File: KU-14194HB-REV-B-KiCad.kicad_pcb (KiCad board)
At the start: 2 copper layers, 387.7 x 180.3 mm, 36 parts, among them U1 CIA_U1, U2 CIA_U2, U20 556, U27 7408_U27, U28 4066_U28, U7 6510_MPU, U8 7406N

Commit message: schematics update
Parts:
- added CN2: USER_PORT_CON, KU-14194HB-RevB-KiCad:EDGE_CON_24P, F.Cu at (39.1, 51.4)
- added FB5: FERRITE_NARROW, KU-14194HB-RevB-KiCad:RECTIFIER, F.Cu at (92.7, 116.8)
- added RP4: R_ARRAY_9WAY_US, KU-14194HB-RevB-KiCad:RP_ARRAY_9WAY, F.Cu at (312.4, 94.0)
- RP3: value R_US_ARRAY -> R_ARRAY_7WAY_US; footprint Resistor_THT:R_Array_SIP8 -> KU-14194HB-RevB-KiCad:RP_ARRAY_7WAY
- moved C2 204.4 mm to (43.2, 73.7), turned to 180 degrees
- moved C96 193.0 mm to (83.8, 71.1), turned to 270 degrees
- moved C3 192.7 mm to (68.6, 73.7)
- moved C9 173.5 mm to (205.7, 73.7), turned to 180 degrees
- moved FB18 32.2 mm to (189.2, 236.2)
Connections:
- net Net-(U1-Pad23) renamed ~CIA1~
- net Net-(U2-Pad2) renamed ~VA14~
- net Net-(U2-Pad23) renamed ~CIA2~
- net Net-(U2-Pad3) renamed ~VA15~
- net Net-(U7-Pad11) renamed /Sheet1/A4
- net Net-(U7-Pad12) renamed /Sheet1/A5
- net Net-(U7-Pad13) renamed /Sheet1/A6
- net Net-(U7-Pad14) renamed /Sheet1/A7
- net Net-(U7-Pad15) renamed /Sheet1/A8
- net Net-(U7-Pad16) renamed /Sheet1/A9
- net Net-(U7-Pad17) renamed /Sheet1/A10
- net Net-(U7-Pad18) renamed /Sheet1/A11
- net Net-(U7-Pad2) renamed RDY
- U1 pad 21: Net-(U1-Pad21) -> ~IRQ~
- U1 pad 22: Net-(U1-Pad22) -> R\~W~
- U1 pad 25: Net-(U1-Pad25) -> PHI2
- U1 pad 26: Net-(U1-Pad26) -> /Sheet1/D7
- U1 pad 27: Net-(U1-Pad27) -> /Sheet1/D6
- U1 pad 28: Net-(U1-Pad28) -> /Sheet1/D5
- U1 pad 29: Net-(U1-Pad29) -> /Sheet1/D4
- U1 pad 30: Net-(U1-Pad30) -> /Sheet1/D3
- U1 pad 31: Net-(U1-Pad31) -> /Sheet1/D2
- U1 pad 32: Net-(U1-Pad32) -> /Sheet1/D1
- U1 pad 33: Net-(U1-Pad33) -> /Sheet1/D0
- U1 pad 35: Net-(U1-Pad35) -> /Sheet1/A3
- U1 pad 36: Net-(U1-Pad36) -> /Sheet1/A2
- U1 pad 37: Net-(U1-Pad37) -> /Sheet1/A1
- U1 pad 38: Net-(U1-Pad38) -> /Sheet1/A0
- U2 pad 22: Net-(U2-Pad22) -> R\~W~
- U2 pad 25: Net-(U2-Pad25) -> PHI2
- U2 pad 26: Net-(U2-Pad26) -> /Sheet1/D7
- U2 pad 27: Net-(U2-Pad27) -> /Sheet1/D6
- U2 pad 28: Net-(U2-Pad28) -> /Sheet1/D5
- U2 pad 29: Net-(U2-Pad29) -> /Sheet1/D4
- U2 pad 30: Net-(U2-Pad30) -> /Sheet1/D3
- U2 pad 31: Net-(U2-Pad31) -> /Sheet1/D2
- U2 pad 32: Net-(U2-Pad32) -> /Sheet1/D1
- U2 pad 33: Net-(U2-Pad33) -> /Sheet1/D0
- U2 pad 35: Net-(U2-Pad35) -> /Sheet1/A3
- U2 pad 36: Net-(U2-Pad36) -> /Sheet1/A2
- U2 pad 37: Net-(U2-Pad37) -> /Sheet1/A1
- U2 pad 38: Net-(U2-Pad38) -> /Sheet1/A0
- U7 pad 10: Net-(U7-Pad10) -> /Sheet1/A3
- U7 pad 19: Net-(U7-Pad19) -> /Sheet1/A12
- U7 pad 20: Net-(U7-Pad20) -> /Sheet1/A13
- U7 pad 22: Net-(U7-Pad22) -> /Sheet1/A14
- U7 pad 23: Net-(U7-Pad23) -> /Sheet1/A15
- U7 pad 3: Net-(U7-Pad3) -> ~IRQ~
- U7 pad 30: Net-(U7-Pad30) -> /Sheet1/D7
- U7 pad 31: Net-(U7-Pad31) -> /Sheet1/D6
- U7 pad 32: Net-(U7-Pad32) -> /Sheet1/D5
- U7 pad 33: Net-(U7-Pad33) -> /Sheet1/D4
- U7 pad 34: Net-(U7-Pad34) -> /Sheet1/D3
- U7 pad 35: Net-(U7-Pad35) -> /Sheet1/D2
- U7 pad 36: Net-(U7-Pad36) -> /Sheet1/D1
- U7 pad 37: Net-(U7-Pad37) -> /Sheet1/D0
- U7 pad 38: Net-(U7-Pad38) -> R\~W~
- U7 pad 39: Net-(U7-Pad39) -> /Sheet1/PH2_FB
- U7 pad 7: Net-(U7-Pad7) -> /Sheet1/A0
- U7 pad 8: Net-(U7-Pad8) -> /Sheet1/A1
- U7 pad 9: Net-(U7-Pad9) -> /Sheet1/A2
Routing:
- net (no net): track 17856.9 -> 16447.7 mm, vias 737 -> 715
- net Net-(U1-Pad33): track 640.6 -> 0.00 mm, vias 15 -> 0
- net /Sheet1/D0: track 0.00 -> 640.6 mm, vias 0 -> 15
- net R\~W~: track 0.00 -> 638.7 mm, vias 0 -> 21
- net Net-(U1-Pad22): track 638.7 -> 0.00 mm, vias 21 -> 0
- net Net-(U1-Pad31): track 609.7 -> 0.00 mm, vias 16 -> 0
- net /Sheet1/D2: track 0.00 -> 609.7 mm, vias 0 -> 16
- net Net-(U1-Pad32): track 599.1 -> 0.00 mm, vias 15 -> 0
- net /Sheet1/D1: track 0.00 -> 599.1 mm, vias 0 -> 15
- net PHI2: track 0.00 -> 596.8 mm, vias 0 -> 7
- net Net-(U1-Pad25): track 596.8 -> 0.00 mm, vias 8 -> 0
- net Net-(U1-Pad38): track 557.4 -> 0.00 mm, vias 17 -> 0
- net /Sheet1/A0: track 0.00 -> 557.4 mm, vias 0 -> 17
- net Net-(U1-Pad36): track 549.0 -> 0.00 mm, vias 16 -> 0
- net /Sheet1/A2: track 0.00 -> 549.0 mm, vias 0 -> 16
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
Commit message: more connectors and stuff
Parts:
- added C1: .1, KU-14194HB-RevB-KiCad:CAP_P5.08mm, F.Cu at (142.2, 71.1)
- added C100: .22, KU-14194HB-RevB-KiCad:CAP_P5.08mm, F.Cu at (381.0, 63.5)
- added C102: 10uF, KU-14194HB-RevB-KiCad:CAP_ELYT_RADIAL_P2.54mm, F.Cu at (363.2, 134.6)
- added C103: .1, KU-14194HB-RevB-KiCad:CAP_P5.08mm, F.Cu at (363.2, 139.7)
- added C18: .1, KU-14194HB-RevB-KiCad:CAP_P5.08mm, F.Cu at (322.6, 104.1)
- added C19: 2200uF, KU-14194HB-RevB-KiCad:LARGE_ELECTROLYTIC_33x18_P38.10mm_AXIAL_TH, F.Cu at (375.9, 132.1)
- added C20: .22, KU-14194HB-RevB-KiCad:CAP_POLY_100V_TH_P10.16mm, F.Cu at (363.2, 88.9)
- added C21: .22, KU-14194HB-RevB-KiCad:CAP_POLY_100V_TH_P10.16mm, F.Cu at (368.3, 114.3)
- added C57: 10uF, KU-14194HB-RevB-KiCad:CAP_ELYT_RADIAL_P2.54mm, F.Cu at (302.3, 203.2)
- added C59: .1, KU-14194HB-RevB-KiCad:CAP_P5.08mm, F.Cu at (297.2, 203.2)
- added C8: 10uF, KU-14194HB-RevB-KiCad:CAP_ELYT_RADIAL_P2.54mm, F.Cu at (193.0, 73.7)
- added C88: 1000uF, KU-14194HB-RevB-KiCad:LARGE_ELECTROLYTIC_33x18_P38.10mm_AXIAL_TH, F.Cu at (350.5, 208.3)
- added C89: .1, KU-14194HB-RevB-KiCad:CAP_P5.08mm, F.Cu at (330.2, 196.8)
- added C90: 470uF, KU-14194HB-RevB-KiCad:LARGE_ELECTROLYTIC_33x18_P38.10mm_AXIAL_TH, F.Cu at (368.3, 208.3)
- added C91: 100uF, KU-14194HB-RevB-KiCad:CAP_ELYT_RADIAL_P5.08mm, F.Cu at (391.2, 205.7)
- added C92: .1, KU-14194HB-RevB-KiCad:CAP_P5.08mm, F.Cu at (391.2, 198.1)
- added C95: .1, KU-14194HB-RevB-KiCad:CAP_P5.08mm, F.Cu at (378.5, 127.0)
- added C97: .22, KU-14194HB-RevB-KiCad:CAP_P5.08mm, F.Cu at (381.0, 68.6)
- added C98: .1, KU-14194HB-RevB-KiCad:CAP_P5.08mm, F.Cu at (383.5, 106.7)
- added C99: .1, KU-14194HB-RevB-KiCad:CAP_P5.08mm, F.Cu at (378.5, 101.6)
- added CN1: KEYBOARD_20PIN_MALE, KU-14194HB-RevB-KiCad:KEYBOARD_CON, F.Cu at (27.9, 129.5)
- added CN3: CASSETTE_PORT_CON, KU-14194HB-RevB-KiCad:EDGE_CON_12P_TAPE, F.Cu at (124.5, 51.5)
- added CN4: SERIAL_BUS_CON, KU-14194HB-RevB-KiCad:SERIAL_CON_DIN6, F.Cu at (180.3, 58.9)
- added CN7: POWER_CON, KU-14194HB-RevB-KiCad:POWER_CON_DIN7, F.Cu at (393.4, 71.6)
- added CN8: CONTROL_PORT, KU-14194HB-RevB-KiCad:JOYPORT_DB9, F.Cu at (391.5, 112.2)
- added CN9: CONTROL_PORT, KU-14194HB-RevB-KiCad:JOYPORT_DB9, F.Cu at (391.5, 144.0)
- added CR2: IN755, KU-14194HB-RevB-KiCad:ZENER_12.7mm, F.Cu at (330.2, 99.1)
- added CR5: 1N4001, KU-14194HB-RevB-KiCad:RECTIFIER_TH_P12.7mm, F.Cu at (335.3, 193.0)
- added CR6: 1N4001, KU-14194HB-RevB-KiCad:RECTIFIER_TH_P12.7mm, F.Cu at (337.8, 205.7)
- added FB1: FERRITE_NARROW, KU-14194HB-RevB-KiCad:FERRITE_BEAD_TH_P12.7mm, F.Cu at (108.0, 76.2)
- added FB2: FERRITE_NARROW, KU-14194HB-RevB-KiCad:FERRITE_BEAD_TH_P12.7mm, F.Cu at (153.7, 71.1)
- added FB20: FERRITE_NARROW, KU-14194HB-RevB-KiCad:FERRITE_BEAD_TH_P12.7mm, F.Cu at (384.8, 188.0)
- added FB21: FERRITE_NARROW, KU-14194HB-RevB-KiCad:FERRITE_BEAD_TH_P12.7mm, F.Cu at (384.8, 182.9)
- added FB3: FERRITE_NARROW, KU-14194HB-RevB-KiCad:FERRITE_BEAD_TH_P12.7mm, F.Cu at (135.9, 76.2)
- added Q1: 2SC1815, KU-14194HB-RevB-KiCad:Q_NPN_ECB, F.Cu at (312.4, 106.7)
- added Q2: 2SC1815, KU-14194HB-RevB-KiCad:Q_NPN_ECB, F.Cu at (335.3, 109.2)
- added Q3: TP298/2SD880, Package_TO_SOT_THT:TO-220-3_Vertical, F.Cu at (307.3, 109.2)
- added R1: 3K3, KU-14194HB-RevB-KiCad:RESISTOR, F.Cu at (124.5, 71.1)
- added R2: 1.5K, KU-14194HB-RevB-KiCad:RESISTOR, F.Cu at (327.7, 99.1)
- added R3: 10K, KU-14194HB-RevB-KiCad:RESISTOR, F.Cu at (342.9, 99.1)
- added R39: 390, KU-14194HB-RevB-KiCad:RESISTOR, F.Cu at (391.2, 193.0)
- added R4: 1K, KU-14194HB-RevB-KiCad:RESISTOR, F.Cu at (340.4, 99.1)
- added R43: 3K3, KU-14194HB-RevB-KiCad:RESISTOR, F.Cu at (147.3, 134.6)
- added R44: 3K3, KU-14194HB-RevB-KiCad:RESISTOR, F.Cu at (147.3, 137.2)
- added R45: 3K3, KU-14194HB-RevB-KiCad:RESISTOR, F.Cu at (147.3, 139.7)
- added VR1: 7812, KU-14194HB-RevB-KiCad:VOTLAGE_REGULATOR_TO220, F.Cu at (309.9, 203.2)
- added VR2: 7805, KU-14194HB-RevB-KiCad:VOTLAGE_REGULATOR_TO220, F.Cu at (373.4, 119.4)
- FB18, FB5, FB7, FB8, FB9: footprint KU-14194HB-RevB-KiCad:RECTIFIER -> KU-14194HB-RevB-KiCad:FERRITE_BEAD_TH_P12.7mm
- moved FB18 204.1 mm to (384.8, 177.8), turned to 180 degrees
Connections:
- net Net-(U7-Pad5) renamed CAEC
- CN2 pad N: (no net) -> Earth
- FB18 pad 2: Net-(CN8-Pad7) -> /Sheet1/5V_joyport
- R36 pad 2: ~RESET~ -> Net-(R36-Pad2)
- U7 pad 24: Net-(U7-Pad24) -> /Sheet1/CASS_MOTOR
- U7 pad 25: Net-(U7-Pad25) -> /Sheet1/CASS_SENSE
- U7 pad 26: Net-(U7-Pad26) -> /Sheet1/CASS_WRT
- U7 pad 27: Net-(U7-Pad27) -> ~CHAREN~
- U7 pad 28: Net-(U7-Pad28) -> ~HIRAM~
- U7 pad 29: Net-(U7-Pad29) -> ~LORAM~
- U8 pad 12: ~RESET~ -> Net-(R36-Pad2)
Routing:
- net (no net): track 16447.7 -> 12520.7 mm, vias 715 -> 556
- net /Sheet1/+9V_UNREG: track 0.00 -> 1275.8 mm, vias 0 -> 49
- net Earth: track 5302.7 -> 4815.6 mm, vias 115 -> 119
- net +5V: track 3523.6 -> 3809.9 mm, vias 107 -> 97
- net Net-(U7-Pad25): track 210.6 -> 0.00 mm, vias 3 -> 0
- net /Sheet1/CASS_SENSE: track 0.00 -> 189.6 mm, vias 0 -> 2
- net Net-(FB2-Pad2): track 0.00 -> 175.0 mm, vias 0 -> 3
- net Net-(U7-Pad26): track 153.9 -> 0.00 mm, vias 2 -> 0
- net /Sheet1/CASS_WRT: track 0.00 -> 153.9 mm, vias 0 -> 1
- net /Sheet1/CAN+5V: track 0.00 -> 144.6 mm, vias 0 -> 6
- net +9V_UNREG: track 0.00 -> 142.4 mm, vias 0 -> 6
- net Net-(U7-Pad24): track 142.2 -> 0.00 mm, vias 2 -> 0
- net /Sheet1/CASS_MOTOR: track 0.00 -> 142.2 mm, vias 0 -> 1
- net +12V: track 0.00 -> 132.6 mm, vias 0 -> 5
- net /Sheet1/9V_UNREG: track 0.00 -> 126.3 mm
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- added copper zone on F.Cu, net Earth

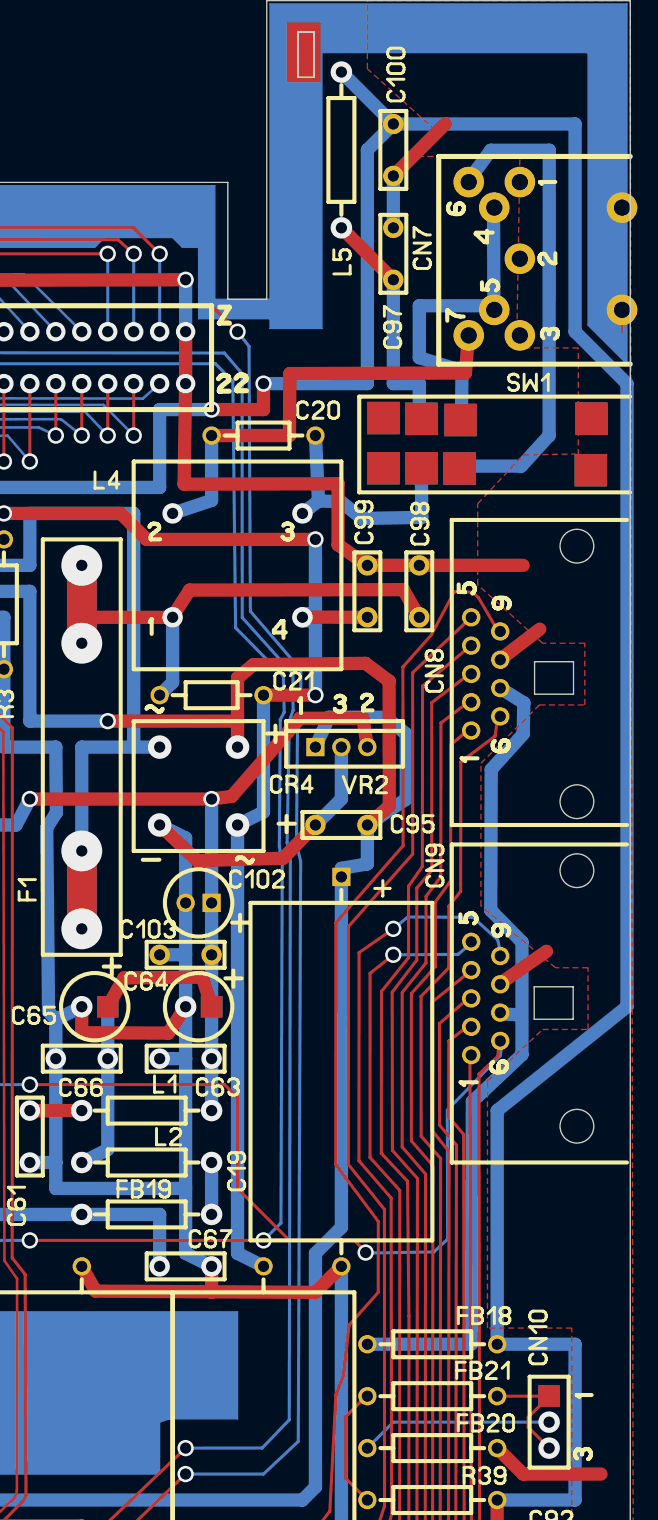
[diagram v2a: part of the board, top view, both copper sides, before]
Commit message: added missing parts. powre connector is upside down in the ku board
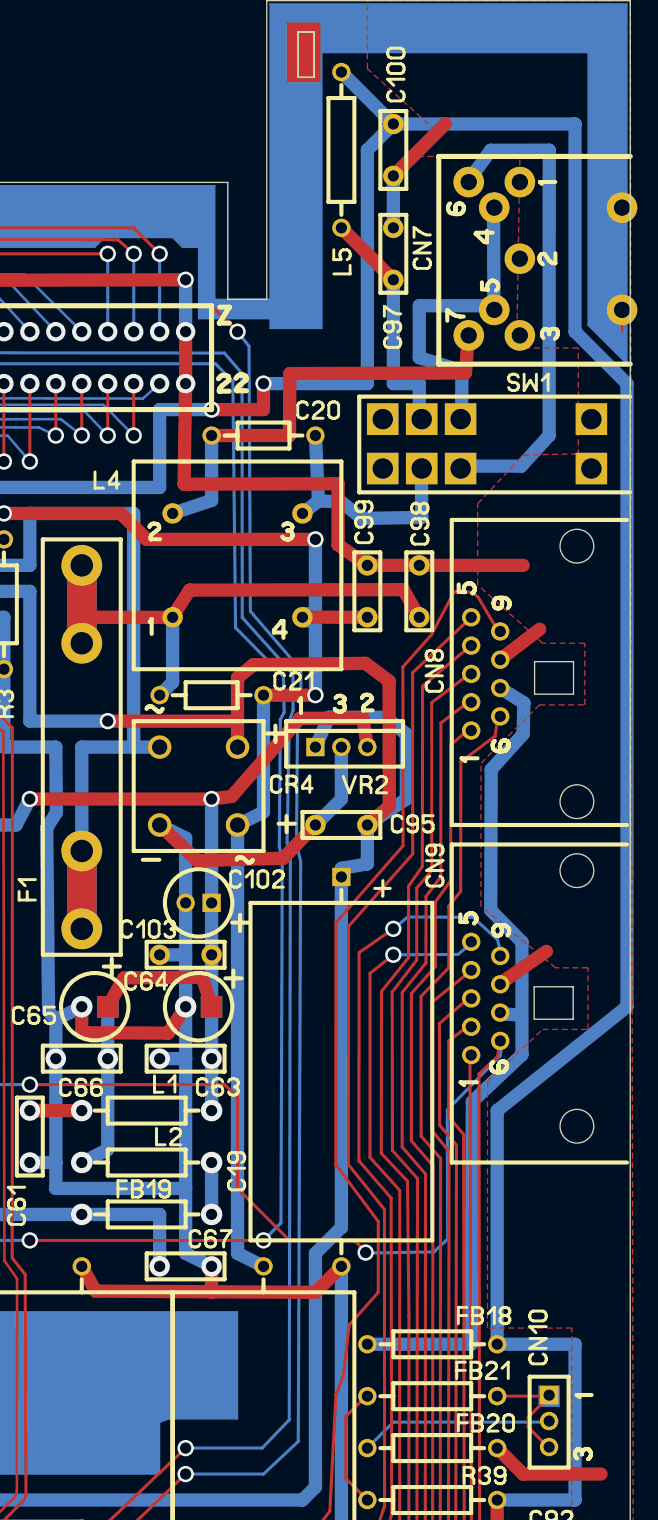
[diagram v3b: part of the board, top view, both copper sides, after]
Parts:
- added CN10: LED_CONNECTOR, KU-14194HB-RevB-KiCad:LED_CON, F.Cu at (396.2, 182.8)
- added CR4: BRIDGE_RECTIFIER, KU-14194HB-RevB-KiCad:BRIDGE_RECTIFIER, F.Cu at (365.8, 119.4)
- added F1: 1A, KU-14194HB-RevB-KiCad:FUSE, F.Cu at (350.5, 137.2)
- added L4: CHOKE, KU-14194HB-RevB-KiCad:CHOKE, F.Cu at (359.4, 106.7)
- added L5: 1.2uH, KU-14194HB-RevB-KiCad:INDUCTOR_P15.24mm, F.Cu at (375.9, 53.3)
- added SW1: POWER_SWITCH, KU-14194HB-RevB-KiCad:POWER_SWITCH, F.Cu at (383.8, 92.1)
- moved C20 10.2 mm to (373.4, 88.9), turned to 180 degrees
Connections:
- C20 pad 1: Net-(C20-Pad1) -> /Sheet1/9VAC
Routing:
- net Net-(C97-Pad2): track 23.7 -> 373.9 mm, vias 1 -> 0
- net (no net): track 12520.7 -> 12170.6 mm
- net /Sheet1/9V_UNREG: track 126.3 -> 268.7 mm, vias 0 -> 5
- net +9V_UNREG: track 142.4 -> 0.00 mm, vias 6 -> 0
- net Net-(C20-Pad1): track 44.9 -> 0.00 mm, vias 1 -> 0
- net /Sheet1/9VAC: track 0.00 -> 23.7 mm
- net Net-(C20-Pad2): track 23.7 -> 44.9 mm, vias 1 -> 0
- net Net-(C21-Pad2): vias 3 -> 0
- net Earth: vias 119 -> 118
- net /Sheet1/LED+: vias 1 -> 0
- net /Sheet1/GND_LED: vias 1 -> 0
- net /Sheet1/9VAC~~: vias 9 -> 7
- net /Sheet1/'9VAC~~: vias 6 -> 3
- net +5V: vias 97 -> 96

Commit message: Oscillator area
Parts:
- added C107: 10uF, KU-14194HB-RevB-KiCad:CAP_ELYT_RADIAL_P2.54mm, F.Cu at (317.5, 167.6)
- added C108: 10uF, KU-14194HB-RevB-KiCad:CAP_ELYT_RADIAL_P2.54mm, F.Cu at (299.7, 165.1)
- added C36: .1, KU-14194HB-RevB-KiCad:RESISTOR, F.Cu at (297.2, 180.3)
- added C56: .1, KU-14194HB-RevB-KiCad:CAP_P5.08mm, F.Cu at (325.1, 124.5)
- added C58: .1, KU-14194HB-RevB-KiCad:CAP_P5.08mm, F.Cu at (322.6, 165.1)
- added C65: 10uF, KU-14194HB-RevB-KiCad:CAP_ELYT_RADIAL_P2.54mm, F.Cu at (353.1, 144.8)
- added C66: .1, KU-14194HB-RevB-KiCad:CAP_P5.08mm, F.Cu at (353.1, 149.9)
- added C67: .1, KU-14194HB-RevB-KiCad:CAP_P5.08mm, F.Cu at (358.1, 170.2)
- added C68: .1, KU-14194HB-RevB-KiCad:CAP_P5.08mm, F.Cu at (309.9, 160.0)
- added C70: ~, KU-14194HB-RevB-KiCad:RESISTOR, F.Cu at (317.5, 185.4)
- added C74: .1, KU-14194HB-RevB-KiCad:CAP_P5.08mm, F.Cu at (309.9, 124.5)
- added C83: 82pF, KU-14194HB-RevB-KiCad:RESISTOR, F.Cu at (315.0, 152.4)
- added C84: .1, KU-14194HB-RevB-KiCad:CAP_P5.08mm, F.Cu at (325.1, 149.9)
- added C85: .47, KU-14194HB-RevB-KiCad:CAP_P5.08mm, F.Cu at (335.3, 144.8)
- added C86: ?, KU-14194HB-RevB-KiCad:RESISTOR, F.Cu at (299.7, 185.4)
- added E1: JUMPER_WIRE, KU-14194HB-RevB-KiCad:JUMPER_WIRE, F.Cu at (279.4, 137.2)
- added FB16: FERRITE_NARROW, KU-14194HB-RevB-KiCad:FERRITE_BEAD_TH_P12.7mm, F.Cu at (281.9, 148.6)
- added FB17: FERRITE_NARROW, KU-14194HB-RevB-KiCad:FERRITE_BEAD_TH_P12.7mm, F.Cu at (290.8, 185.4)
- added FB19: FERRITE_NARROW, KU-14194HB-RevB-KiCad:FERRITE_BEAD_TH_P12.7mm, F.Cu at (356.9, 165.1)
- added Q7: 2SC1815, KU-14194HB-RevB-KiCad:Q_NPN_ECB, F.Cu at (327.7, 154.9)
- added R16: 1K, KU-14194HB-RevB-KiCad:RESISTOR, F.Cu at (332.7, 124.5)
- added R17: 2K7, KU-14194HB-RevB-KiCad:RESISTOR, F.Cu at (335.3, 124.5)
- added R19: 15K, KU-14194HB-RevB-KiCad:RESISTOR, F.Cu at (332.7, 152.4)
- added R26: 100, KU-14194HB-RevB-KiCad:RESISTOR, F.Cu at (335.3, 172.7)
- added R27: 500, KU-14194HB-RevB-KiCad:POTMETER, F.Cu at (332.7, 160.0)
- added R52: ?, KU-14194HB-RevB-KiCad:RESISTOR, F.Cu at (335.3, 170.2)
- added R53: ?, KU-14194HB-RevB-KiCad:RESISTOR, F.Cu at (322.6, 167.6)
- added U29: 74LS74, KU-14194HB-RevB-KiCad:DIP14, F.Cu at (290.8, 137.2)
- added U30: 74LS193, KU-14194HB-RevB-KiCad:DIP16, F.Cu at (308.6, 138.4)
- added U31: 74LS629N, KU-14194HB-RevB-KiCad:DIP16, F.Cu at (308.6, 174.0)
- added U32: MC4044, KU-14194HB-RevB-KiCad:DIP14, F.Cu at (323.9, 137.2)
- added Y1: Crystal, KU-14194HB-RevB-KiCad:CRYSTAL, F.Cu at (320.0, 180.3)
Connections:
- R36 pad 2: Net-(R36-Pad2) -> ~RESET~
- U7 pad 1: Net-(U7-Pad1) -> PHI_0
- U8 pad 12: Net-(R36-Pad2) -> ~RESET~
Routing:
- net /Sheet1/+9V_UNREG: track 1275.8 -> 0.00 mm, vias 49 -> 0
- net Earth: track 4815.6 -> 5978.7 mm, vias 118 -> 136
- net (no net): track 12170.6 -> 11054.7 mm, vias 556 -> 442
- net /Sheet1/+Vc: track 0.00 -> 314.6 mm, vias 0 -> 11
- net PHI_0: track 0.00 -> 270.1 mm, vias 0 -> 4
- net Net-(U7-Pad1): track 270.1 -> 0.00 mm, vias 5 -> 0
- net DOT_CLOCK: track 0.00 -> 148.4 mm, vias 0 -> 4
- net Net-(FB16-Pad1): track 0.00 -> 105.8 mm, vias 0 -> 4
- net PHI_COLOR: track 0.00 -> 79.0 mm, vias 0 -> 2
- net Net-(R16-Pad2): track 0.00 -> 74.5 mm, vias 0 -> 1
- net /Sheet1/jumper_select: track 0.00 -> 51.4 mm, vias 0 -> 2
- net Net-(C108-Pad1): track 0.00 -> 43.1 mm, vias 0 -> 1
- net Net-(U29-Pad9): track 0.00 -> 38.0 mm, vias 0 -> 1
- net Net-(U29-Pad5): track 0.00 -> 35.5 mm, vias 0 -> 1
- net /Sheet1/CAN+5V: track 144.6 -> 175.3 mm
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
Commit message: More schematics
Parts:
- added C25: .1, KU-14194HB-RevB-KiCad:CAP_P5.08mm, F.Cu at (53.3, 170.2)
- added C26: .1, KU-14194HB-RevB-KiCad:CAP_P5.08mm, F.Cu at (68.6, 170.2)
- added C27: .1, KU-14194HB-RevB-KiCad:CAP_P5.08mm, F.Cu at (83.8, 170.2)
- added C28: .1, KU-14194HB-RevB-KiCad:CAP_P5.08mm, F.Cu at (99.1, 170.2)
- added C29: .1, KU-14194HB-RevB-KiCad:CAP_P5.08mm, F.Cu at (116.8, 170.2)
- added C40: .1, KU-14194HB-RevB-KiCad:CAP_P5.08mm, F.Cu at (53.3, 208.3)
- added C41: .1, KU-14194HB-RevB-KiCad:CAP_P5.08mm, F.Cu at (68.6, 208.3)
- added C42: .1, KU-14194HB-RevB-KiCad:CAP_P5.08mm, F.Cu at (83.8, 208.3)
- added C43: .1, KU-14194HB-RevB-KiCad:CAP_P5.08mm, F.Cu at (99.1, 208.3)
- added C44: .1, KU-14194HB-RevB-KiCad:CAP_P5.08mm, F.Cu at (116.8, 208.3)
- added L2: 2.2uH, KU-14194HB-RevB-KiCad:RESISTOR, F.Cu at (350.5, 160.0)
- added R31: 180, KU-14194HB-RevB-KiCad:RESISTOR, F.Cu at (124.5, 180.3)
- added R42: ~, KU-14194HB-RevB-KiCad:RESISTOR, F.Cu at (203.2, 195.6)
- added RP1: 33, KU-14194HB-RevB-KiCad:RP_ARRAY_7WAY, F.Cu at (111.8, 147.3)
- added RP2: 33, KU-14194HB-RevB-KiCad:RP_ARRAY_7WAY, F.Cu at (111.8, 185.4)
- added U10: 4164-2, KU-14194HB-RevB-KiCad:DIP16, F.Cu at (72.4, 156.2)
- added U11: 4164-2, KU-14194HB-RevB-KiCad:DIP16, F.Cu at (87.6, 156.2)
- added U12: 4164-2, KU-14194HB-RevB-KiCad:DIP16, F.Cu at (102.9, 156.2)
- added U13: 74LS257, KU-14194HB-RevB-KiCad:DIP16, F.Cu at (120.7, 156.2)
- added U21: 4164-2, KU-14194HB-RevB-KiCad:DIP16, F.Cu at (57.1, 194.3)
- added U22: 4164-2, KU-14194HB-RevB-KiCad:DIP16, F.Cu at (72.4, 194.3)
- added U23: 4164-2, KU-14194HB-RevB-KiCad:DIP16, F.Cu at (87.6, 194.3)
- added U24: 4164-2, KU-14194HB-RevB-KiCad:DIP16, F.Cu at (102.9, 194.3)
- added U25: 74LS257, KU-14194HB-RevB-KiCad:DIP16, F.Cu at (120.7, 194.3)
- added U9: 4164-2, KU-14194HB-RevB-KiCad:DIP16, F.Cu at (57.1, 156.2)
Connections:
- net /Sheet1/A0 renamed A0
- net /Sheet1/A1 renamed A1
- net /Sheet1/A12 renamed A12
- net /Sheet1/A13 renamed A13
- net /Sheet1/A14 renamed A14
- net /Sheet1/A15 renamed A15
- net /Sheet1/A2 renamed A2
- net /Sheet1/A3 renamed A3
- net /Sheet1/D0 renamed D0
- net /Sheet1/D1 renamed D1
- net /Sheet1/D2 renamed D2
- net /Sheet1/D3 renamed D3
- net /Sheet1/D4 renamed D4
- net /Sheet1/D5 renamed D5
- net /Sheet1/D6 renamed D6
- net /Sheet1/D7 renamed D7
- net /Sheet1/~NMI~ renamed ~NMI~
- U7 pad 11: /Sheet1/A4 -> A4
- U7 pad 12: /Sheet1/A5 -> A5
- U7 pad 13: /Sheet1/A6 -> A6
- U7 pad 14: /Sheet1/A7 -> A7
- U7 pad 15: /Sheet1/A8 -> A8
- U7 pad 16: /Sheet1/A9 -> A9
- U7 pad 17: /Sheet1/A10 -> A10
- U7 pad 18: /Sheet1/A11 -> A11
- U8 pad 10: (no net) -> /Sheet5D659BBD/~AEC~
- U8 pad 11: (no net) -> Net-(U8-Pad11)
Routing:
- net (no net): track 11054.7 -> 7123.8 mm, vias 442 -> 266
- net A8: track 0.00 -> 729.2 mm, vias 0 -> 16
- net /Sheet1/A8: track 729.2 -> 0.00 mm, vias 17 -> 0
- net A9: track 0.00 -> 675.7 mm, vias 0 -> 15
- net /Sheet1/A9: track 675.7 -> 0.00 mm, vias 16 -> 0
- net A10: track 0.00 -> 674.8 mm, vias 0 -> 16
- net /Sheet1/A10: track 674.8 -> 0.00 mm, vias 17 -> 0
- net A11: track 0.00 -> 615.7 mm, vias 0 -> 17
- net /Sheet1/A11: track 615.7 -> 0.00 mm, vias 18 -> 0
- net A4: track 0.00 -> 516.8 mm, vias 0 -> 12
- net /Sheet1/A4: track 516.8 -> 0.00 mm, vias 13 -> 0
- net A5: track 0.00 -> 453.6 mm, vias 0 -> 12
- net /Sheet1/A5: track 453.6 -> 0.00 mm, vias 13 -> 0
- net A6: track 0.00 -> 449.3 mm, vias 0 -> 8
- net /Sheet1/A6: track 449.3 -> 0.00 mm, vias 9 -> 0
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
